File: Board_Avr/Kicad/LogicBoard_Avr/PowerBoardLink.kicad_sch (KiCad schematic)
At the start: 7 parts, among them J4 Power board connector

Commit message: Finalised routing
Signed-off-by: bebenlebricolo <benoittarrade@hotmail.fr>
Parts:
- added R10, R7, R8, R9: 33, Resistor_SMD:R_0402_1005Metric_Pad0.72x0.64mm_HandSolder, symbol Device:R
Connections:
- net OC1A_PWM: now also R7.1; no longer J4.2 (Pin_2), JP6.1 (A)
- net OC1B_PWM: now also R8.1; no longer JP2.1 (A), JP4.1 (A), JP7.1 (A)
- net OC2A_PWM: now also R9.1; no longer JP3.1 (A)
- net OC2B_PWM: now also R10.1; no longer JP5.1 (A)
- new net OC1A_PWM_OUT: J4.2 (Pin_2), JP6.1 (A), R7.2
- new net OC1B_PWM_OUT: JP2.1 (A), JP4.1 (A), JP7.1 (A), R8.2
- new net OC2A_PWM_OUT: JP3.1 (A), R9.2
- new net OC2B_PWM_OUT: JP5.1 (A), R10.2
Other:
- note added: "OC1A_PWM_OUT for both"
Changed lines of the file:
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@@
-    (stroke (width 0) (type default) (color 0 0 0 0))
-  )
-  (wire (pts (xy 165.1 47.625) (xy 168.91 47.625))
     (stroke (width 0) (type default) (color 0 0 0 0))
   )
@@
     (stroke (width 0) (type default) (color 0 0 0 0))
   )
-  (wire (pts (xy 48.895 47.625) (xy 51.435 47.625))
-    (stroke (width 0) (type default) (color 0 0 0 0))
-  )
   (polyline (pts (xy 46.355 127) (xy 104.14 127))
     (stroke (width 0) (type default) (color 0 0 0 0))
@@
     (stroke (width 0) (type default) (color 0 0 0 0))
   )
-  (wire (pts (xy 165.1 50.165) (xy 168.91 50.165))
-    (stroke (width 0) (type default) (color 0 0 0 0))
-  )
   (polyline (pts (xy 31.75 63.5) (xy 120.015 63.5))
     (stroke (width 0) (type default) (color 0 0 0 0))
@@
     (stroke (width 0) (type default) (color 0 0 0 0))
   )
-  (wire (pts (xy 165.1 52.705) (xy 168.91 52.705))
-    (stroke (width 0) (type default) (color 0 0 0 0))
-  )
   (polyline (pts (xy 120.015 58.42) (xy 120.015 59.055))
     (stroke (width 0) (type default) (color 0 0 0 0))
@@
   )
   (polyline (pts (xy 31.75 33.02) (xy 120.015 33.02))
-    (stroke (width 0) (type default) (color 0 0 0 0))
-  )
-  (wire (pts (xy 165.1 45.085) (xy 168.91 45.085))
     (stroke (width 0) (type default) (color 0 0 0 0))
   )
@@
     (effects (font (size 1.27 1.27) italic) (justify left bottom))
   )
+  (text "OC1A_PWM_OUT for both" (at 40.64 50.165 0)
+    (effects (font (size 1.27 1.27)) (justify left bottom))
+  )
   (text "oc2b" (at 85.725 123.825 0)
     (effects (font (size 1.27 1.27) italic) (justify left bottom))
@@
     (effects (font (size 1.27 1.27) italic) (justify left bottom))
   )
-  (label "HBridgeAHO" (at 51.435 47.625 0)
-    (effects (font (size 1.27 1.27)) (justify left bottom))
-  )
   (label "HBridgeALO" (at 165.1 74.93 180)
     (effects (font (size 1.27 1.27)) (justify right bottom))
   )
-  (label "OC2A_PWM" (at 168.91 50.165 0)
+  (label "OC2A_PWM_OUT" (at 174.625 36.195 0)
     (effects (font (size 1.27 1.27)) (justify left bottom))
   )
@@
     (effects (font (size 1.27 1.27)) (justify left bottom))
   )
-  (label "OC1B_PWM" (at 168.91 47.625 0)
-    (effects (font (size 1.27 1.27)) (justify left bottom))
-  )
-  (label "HBridgeAHO" (at 165.1 72.39 180)
-    (effects (font (size 1.27 1.27)) (justify right bottom))
+  (label "OC1B_PWM_OUT" (at 174.625 28.575 0)
+    (effects (font (size 1.27 1.27)) (justify left bottom))
   )
   (label "HBridgeBHO" (at 105.41 48.895 0)
     (effects (font (size 1.27 1.27)) (justify left bottom))
   )
-  (label "OC1A_PWM" (at 90.805 71.12 180)
-    (effects (font (size 1.27 1.27)) (justify right bottom))
-  )
-  (label "OC1A_PWM" (at 168.91 45.085 0)
-    (effects (font (size 1.27 1.27)) (justify left bottom))
-  )
-  (label "OC2B_PWM" (at 168.91 52.705 0)
-    (effects (font (size 1.27 1.27)) (justify left bottom))
-  )
-  (label "OC2B_PWM" (at 89.535 52.07 180)
+  (label "OC1A_PWM_OUT" (at 90.805 71.12 180)
+    (effects (font (size 1.27 1.27)) (justify right bottom))
+  )
+  (label "OC1A_PWM_OUT" (at 174.625 20.955 0)
+    (effects (font (size 1.27 1.27)) (justify left bottom))
+  )
+  (label "OC2B_PWM_OUT" (at 174.625 43.815 0)
+    (effects (font (size 1.27 1.27)) (justify left bottom))
+  )
+  (label "OC2B_PWM_OUT" (at 89.535 52.07 180)
     (effects (font (size 1.27 1.27)) (justify right bottom))
   )
@@
     (effects (font (size 1.27 1.27)) (justify left bottom))
   )
-  (label "OC2A_PWM" (at 45.085 76.835 180)
-    (effects (font (size 1.27 1.27)) (justify right bottom))
-  )
-  (label "OC1A_PWM" (at 48.895 47.625 180)
-    (effects (font (size 1.27 1.27)) (justify right bottom))
-  )
-  (label "OC1B_PWM" (at 90.805 76.835 180)
-    (effects (font (size 1.27 1.27)) (justify right bottom))
-  )
-  (label "OC1B_PWM" (at 89.535 46.355 180)
-    (effects (font (size 1.27 1.27)) (justify right bottom))
-  )
-  (label "OC1B_PWM" (at 45.085 71.12 180)
+  (label "OC2A_PWM_OUT" (at 45.085 76.835 180)
+    (effects (font (size 1.27 1.27)) (justify right bottom))
+  )
+  (label "OC1B_PWM_OUT" (at 90.805 76.835 180)
+    (effects (font (size 1.27 1.27)) (justify right bottom))
+  )
+  (label "OC1B_PWM_OUT" (at 89.535 46.355 180)
+    (effects (font (size 1.27 1.27)) (justify right bottom))
+  )
+  (label "OC1B_PWM_OUT" (at 45.085 71.12 180)
     (effects (font (size 1.27 1.27)) (justify right bottom))
   )
@@
     (effects (font (size 1.27 1.27)) (justify right bottom))
   )
+  (label "OC1A_PWM_OUT" (at 165.1 72.39 180)
+    (effects (font (size 1.27 1.27)) (justify right bottom))
+  )
   (label "HBridgeBHO" (at 165.1 77.47 180)
     (effects (font (size 1.27 1.27)) (justify right bottom))
   )
-  (hierarchical_label "OC1A_PWM" (shape input) (at 165.1 45.085 180)
+  (hierarchical_label "OC1A_PWM" (shape input) (at 167.005 20.955 180)
     (effects (font (size 1.27 1.27)) (justify right))
   )
@@
     (effects (font (size 1.27 1.27)) (justify right))
   )
-  (hierarchical_label "OC2A_PWM" (shape input) (at 165.1 50.165 180)
-    (effects (font (size 1.27 1.27)) (justify right))
-  )
-  (hierarchical_label "OC2B_PWM" (shape input) (at 165.1 52.705 180)
-    (effects (font (size 1.27 1.27)) (justify right))
-  )
-  (hierarchical_label "OC1B_PWM" (shape input) (at 165.1 47.625 180)
+  (hierarchical_label "OC2A_PWM" (shape input) (at 167.005 36.195 180)
+    (effects (font (size 1.27 1.27)) (justify right))
+  )
+  (hierarchical_label "OC2B_PWM" (shape input) (at 167.005 43.815 180)
+    (effects (font (size 1.27 1.27)) (justify right))
+  )
+  (hierarchical_label "OC1B_PWM" (shape input) (at 167.005 28.575 180)
     (effects (font (size 1.27 1.27)) (justify right))
   )
@@
     (pin "7")
   )
+  (symbol (lib_id "Device:R") (at 170.815 28.575 90) (unit 1)
+    (in_bom yes) (on_board yes) (fields_autoplaced)
+    (property "Reference" "R8" (id 0) (at 170.815 23.5925 90))
+    (property "Value" "33" (id 1) (at 170.815 26.3676 90))
+    (property "Footprint" "Resistor_SMD:R_0402_1005Metric_Pad0.72x0.64mm_HandSolder" (id 2) (at 170.815 30.353 90)
+      (effects (font (size 1.27 1.27)) hide)
+    )
+    (property "Datasheet" "~" (id 3) (at 170.815 28.575 0)
+      (effects (font (size 1.27 1.27)) hide)
+    )
+    (pin "1")
+    (pin "2")
+  )
+  (symbol (lib_id "Device:R") (at 170.815 20.955 90) (unit 1)
+    (in_bom yes) (on_board yes) (fields_autoplaced)
+    (property "Reference" "R7" (id 0) (at 170.815 15.9725 90))
+    (property "Value" "33" (id 1) (at 170.815 18.7476 90))
+    (property "Footprint" "Resistor_SMD:R_0402_1005Metric_Pad0.72x0.64mm_HandSolder" (id 2) (at 170.815 22.733 90)
+      (effects (font (size 1.27 1.27)) hide)
+    )
+    (property "Datasheet" "~" (id 3) (at 170.815 20.955 0)
+      (effects (font (size 1.27 1.27)) hide)
+    )
+    (pin "1")
+    (pin "2")
+  )
   (symbol (lib_id "Jumper:SolderJumper_2_Open") (at 94.615 46.355 0) (unit 1)
     (in_bom yes) (on_board yes)
@@
     (pin "2")
   )
+  (symbol (lib_id "Device:R") (at 170.815 43.815 90) (unit 1)
+    (in_bom yes) (on_board yes) (fields_autoplaced)
+    (property "Reference" "R10" (id 0) (at 170.815 38.8325 90))
+    (property "Value" "33" (id 1) (at 170.815 41.6076 90))
+    (property "Footprint" "Resistor_SMD:R_0402_1005Metric_Pad0.72x0.64mm_HandSolder" (id 2) (at 170.815 45.593 90)
+      (effects (font (size 1.27 1.27)) hide)
+    )
+    (property "Datasheet" "~" (id 3) (at 170.815 43.815 0)
+      (effects (font (size 1.27 1.27)) hide)
+    )
+    (pin "1")
+    (pin "2")
+  )
   (symbol (lib_id "power:GND") (at 162.56 85.09 0) (unit 1)
     (in_bom yes) (on_board yes) (fields_autoplaced)
@@
     (pin "1")
   )
+  (symbol (lib_id "Device:R") (at 170.815 36.195 90) (unit 1)
+    (in_bom yes) (on_board yes) (fields_autoplaced)
+    (property "Reference" "R9" (id 0) (at 170.815 31.2125 90))
+    (property "Value" "33" (id 1) (at 170.815 33.9876 90))
+    (property "Footprint" "Resistor_SMD:R_0402_1005Metric_Pad0.72x0.64mm_HandSolder" (id 2) (at 170.815 37.973 90)
+      (effects (font (size 1.27 1.27)) hide)
+    )
+    (property "Datasheet" "~" (id 3) (at 170.815 36.195 0)
+      (effects (font (size 1.27 1.27)) hide)
+    )
+    (pin "1")
+    (pin "2")
+  )
 )

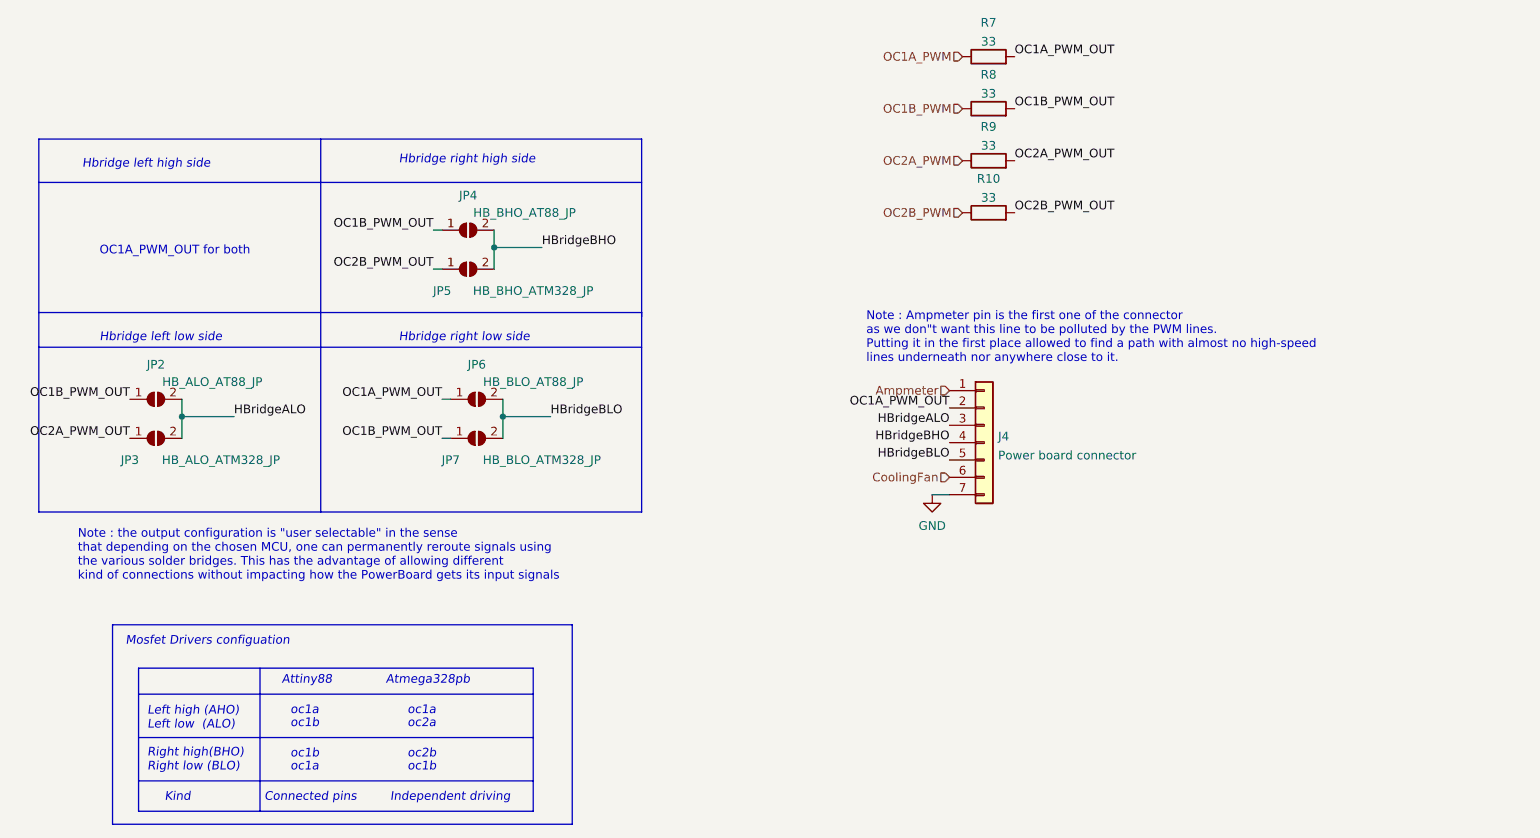
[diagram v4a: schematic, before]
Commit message: Fixed silkscreen and added PWM signal test points
Signed-off-by: bebenlebricolo <benoittarrade@hotmail.fr>
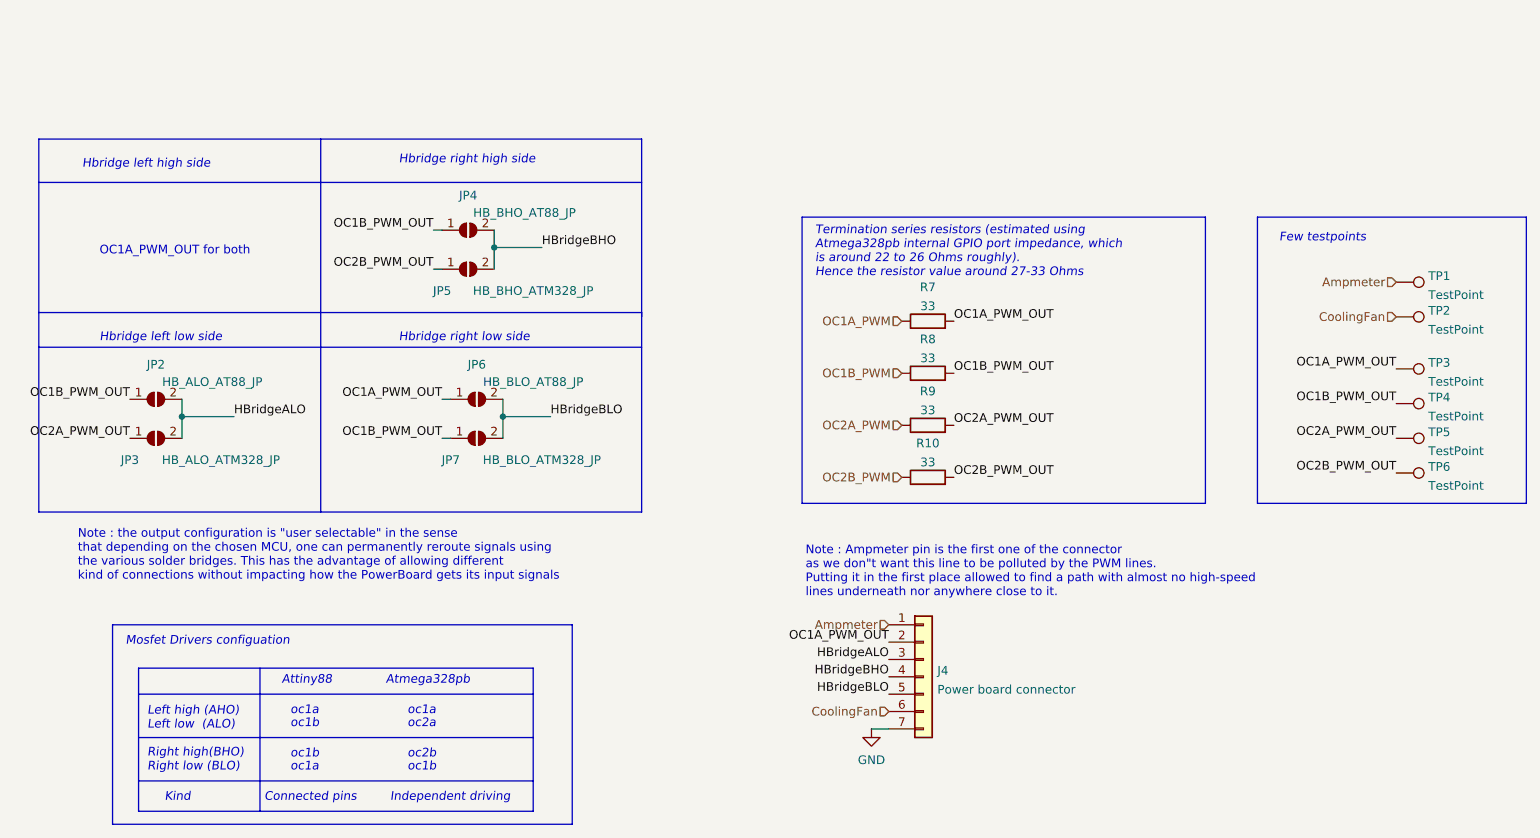
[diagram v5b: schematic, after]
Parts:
- added TP1, TP2, TP3, TP4, TP5, TP6: TestPoint, TestPoint:TestPoint_Pad_D1.0mm, symbol Connector:TestPoint
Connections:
- net Ampmeter: now also TP1.1
- net CoolingFan: now also TP2.1
- net OC1A_PWM_OUT: now also TP3.1
- net OC1B_PWM_OUT: now also TP4.1
- net OC2A_PWM_OUT: now also TP5.1
- net OC2B_PWM_OUT: now also TP6.1
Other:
- note added: "Few testpoints"
- note added: "Termination series resistors (estimated using Atmega328pb internal GPIO port impedance, which is around 22 to 26 Ohms roughly). Hence the resistor value around 27-33 Ohms"
- moved on the sheet: J4, R10, R7, R8, R9
